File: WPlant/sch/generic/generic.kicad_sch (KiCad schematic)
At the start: 70 parts, among them J1 PROG/JTAG, J10 Ext, J8 eInk-Buttons, J9 Leak, M1 Motor_DC, Q5 PMOS, Q6 NPN, SW1 SW_Push, SW2 SW_Push, SW3 SW_Push, U1 SIWG917Y121MGABAR, U10 SP485EEN-L/TR, U11 TXU0102QDCURQ1, U5 TC4427AEOA713, U8 NC7S02P5, U9 INA180A2, X1 SIT1552AI-JE-DCC-32.768D

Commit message: Update WP Extension and Generic
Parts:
- removed Q5: PMOS, symbol Simulation_SPICE:PMOS
- removed Q6: NPN, symbol Simulation_SPICE:NPN
- added Q6: Si2301, Package_TO_SOT_SMD:SOT-23, symbol Device:Q_PMOS_GSD
- added Q7: BC817, Package_TO_SOT_SMD:SOT-23, symbol Transistor_BJT:BC817
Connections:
- net GND: now also Q7.2 (E)
- net VBUS: now also Q6.2 (S)
- net at R36.1: now also Q6.3 (D)
- net at R38.1: now also Q6.1 (G), Q7.3 (C)
- net at R39.1: now also Q7.1 (B)
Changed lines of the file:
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@@
 	)
 	(symbol
-		(lib_id "Simulation_SPICE:PMOS")
-		(at 66.04 149.86 270)
-		(mirror x)
-		(unit 1)
-		(exclude_from_sim no)
-		(in_bom yes)
-		(on_board yes)
-		(dnp no)
-		(property "Reference" "Q5"
-			(at 66.04 140.97 90)
-			(effects
-				(font
-					(size 1.27 1.27)
-				)
-			)
-		)
-		(property "Value" "PMOS"
-			(at 66.04 143.51 90)
-			(effects
-				(font
-					(size 1.27 1.27)
-				)
-			)
-		)
-		(property "Footprint" ""
-			(at 68.58 144.78 0)
-			(effects
-				(font
-					(size 1.27 1.27)
-				)
-				(hide yes)
-			)
-		)
-		(property "Datasheet" "https://ngspice.sourceforge.io/docs/ngspice-html-manual/manual.xhtml#cha_MOSFETs"
-			(at 53.34 149.86 0)
-			(effects
-				(font
-					(size 1.27 1.27)
-				)
-				(hide yes)
-			)
-		)
-		(property "Description" "P-MOSFET transistor, drain/source/gate"
-			(at 66.04 149.86 0)
-			(effects
-				(font
-					(size 1.27 1.27)
-				)
-				(hide yes)
-			)
-		)
-		(property "Sim.Device" "PMOS"
-			(at 48.895 149.86 0)
-			(effects
-				(font
-					(size 1.27 1.27)
-				)
-				(hide yes)
-			)
-		)
-		(property "Sim.Type" "VDMOS"
-			(at 46.99 149.86 0)
-			(effects
-				(font
-					(size 1.27 1.27)
-				)
-				(hide yes)
-			)
-		)
-		(property "Sim.Pins" "1=D 2=G 3=S"
-			(at 50.8 149.86 0)
-			(effects
-				(font
-					(size 1.27 1.27)
-				)
-				(hide yes)
-			)
-		)
-		(pin "2"
-		)
-		(pin "1"
-		)
-		(pin "3"
-		)
-		(instances
-			(project ""
-				(path "/71bd3f7f-463d-4a2c-bec7-ca56c2fe6cec"
-					(reference "Q5")
-					(unit 1)
-				)
-			)
-		)
-	)
-	(symbol
 		(lib_id "Device:R")
 		(at 190.5 97.79 90)
@@
 	)
 	(symbol
-		(lib_id "Simulation_SPICE:NPN")
-		(at 29.21 171.45 0)
-		(unit 1)
-		(exclude_from_sim no)
-		(in_bom yes)
-		(on_board yes)
-		(dnp no)
-		(fields_autoplaced yes)
-		(property "Reference" "Q6"
-			(at 34.29 170.1799 0)
-			(effects
-				(font
-					(size 1.27 1.27)
-				)
-				(justify left)
-			)
-		)
-		(property "Value" "NPN"
-			(at 34.29 172.7199 0)
-			(effects
-				(font
-					(size 1.27 1.27)
-				)
-				(justify left)
-			)
-		)
-		(property "Footprint" ""
-			(at 92.71 171.45 0)
-			(effects
-				(font
-					(size 1.27 1.27)
-				)
-				(hide yes)
-			)
-		)
-		(property "Datasheet" "https://ngspice.sourceforge.io/docs/ngspice-html-manual/manual.xhtml#cha_BJTs"
-			(at 92.71 171.45 0)
-			(effects
-				(font
-					(size 1.27 1.27)
-				)
-				(hide yes)
-			)
-		)
-		(property "Description" "Bipolar transistor symbol for simulation only, substrate tied to the emitter"
-			(at 29.21 171.45 0)
-			(effects
-				(font
-					(size 1.27 1.27)
-				)
-				(hide yes)
-			)
-		)
-		(property "Sim.Device" "NPN"
-			(at 29.21 171.45 0)
-			(effects
-				(font
-					(size 1.27 1.27)
-				)
-				(hide yes)
-			)
-		)
-		(property "Sim.Type" "GUMMELPOON"
-			(at 29.21 171.45 0)
-			(effects
-				(font
-					(size 1.27 1.27)
-				)
-				(hide yes)
-			)
-		)
-		(property "Sim.Pins" "1=C 2=B 3=E"
-			(at 29.21 171.45 0)
-			(effects
-				(font
-					(size 1.27 1.27)
-				)
-				(hide yes)
-			)
-		)
-		(pin "3"
-		)
-		(pin "1"
-		)
-		(pin "2"
-		)
-		(instances
-			(project ""
-				(path "/71bd3f7f-463d-4a2c-bec7-ca56c2fe6cec"
-					(reference "Q6")
-					(unit 1)
-				)
-			)
-		)
-	)
-	(symbol
 		(lib_id "power:+3.3V")
 		(at 52.07 88.9 270)
@@
 	)
 	(symbol
+		(lib_id "Device:Q_PMOS_GSD")
+		(at 66.04 149.86 270)
+		(mirror x)
+		(unit 1)
+		(exclude_from_sim no)
+		(in_bom yes)
+		(on_board yes)
+		(dnp no)
+		(property "Reference" "Q6"
+			(at 66.04 140.97 90)
+			(effects
+				(font
+					(size 1.27 1.27)
+				)
+			)
+		)
+		(property "Value" "Si2301"
+			(at 66.04 143.51 90)
+			(effects
+				(font
+					(size 1.27 1.27)
+				)
+			)
+		)
+		(property "Footprint" "Package_TO_SOT_SMD:SOT-23"
+			(at 68.58 144.78 0)
+			(effects
+				(font
+					(size 1.27 1.27)
+				)
+				(hide yes)
+			)
+		)
+		(property "Datasheet" "~"
+			(at 66.04 149.86 0)
+			(effects
+				(font
+					(size 1.27 1.27)
+				)
+				(hide yes)
+			)
+		)
+		(property "Description" "P-MOSFET transistor, gate/source/drain"
+			(at 66.04 149.86 0)
+			(effects
+				(font
+					(size 1.27 1.27)
+				)
+				(hide yes)
+			)
+		)
+		(pin "2"
+		)
+		(pin "1"
+		)
+		(pin "3"
+		)
+		(instances
+			(project ""
+				(path "/71bd3f7f-463d-4a2c-bec7-ca56c2fe6cec"
+					(reference "Q6")
+					(unit 1)
+				)
+			)
+		)
+	)
+	(symbol
 		(lib_id "power:+3.3V")
 		(at 39.37 19.05 0)
@@
 					(unit 1)
 				)
+			)
+		)
+	)
+	(symbol
+		(lib_id "Transistor_BJT:BC817")
+		(at 29.21 171.45 0)
+		(unit 1)
+		(exclude_from_sim no)
+		(in_bom yes)
+		(on_board yes)
+		(dnp no)
+		(property "Reference" "Q7"
+			(at 34.798 169.672 0)
+			(effects
+				(font
+					(size 1.27 1.27)
+				)
+				(justify left)
+			)
+		)
+		(property "Value" "BC817"
+			(at 33.782 174.498 0)
+			(effects
+				(font
+					(size 1.27 1.27)
+				)
+				(justify left)
+			)
+		)
+		(property "Footprint" "Package_TO_SOT_SMD:SOT-23"
+			(at 34.29 173.355 0)
+			(effects
+				(font
+					(size 1.27 1.27)
+					(italic yes)
+				)
+				(justify left)
+				(hide yes)
+			)
+		)
+		(property "Datasheet" "https://www.onsemi.com/pub/Collateral/BC818-D.pdf"
+			(at 29.21 171.45 0)
+			(effects
+				(font
+					(size 1.27 1.27)
+				)
+				(justify left)
+				(hide yes)
+			)
+		)
+		(property "Description" "0.8A Ic, 45V Vce, NPN Transistor, SOT-23"
+			(at 29.21 171.45 0)
+			(effects
+				(font
+					(size 1.27 1.27)
+				)
+				(hide yes)
+			)
+		)
+		(pin "1"
+		)
+		(pin "2"
+		)
+		(pin "3"
+		)
+		(instances
+			(project ""
+				(path "/71bd3f7f-463d-4a2c-bec7-ca56c2fe6cec"
+					(reference "Q7")
+					(unit 1)
+				)

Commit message: Almost finished WP Generic
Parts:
- C1, C2, C3, C30, C31, C32, C33, C35, C36, C37, C38, C39, C4, C5, C6, C7, C8, C9: footprint (none) -> Capacitor_SMD:C_0603_1608Metric_Pad1.08x0.95mm_HandSolder
- D1, D2: footprint (none) -> LED_THT:LED_D5.0mm
- D10: footprint (none) -> Diode_SMD:D_SMC
- J1: footprint (none) -> Connector_PinHeader_2.54mm:PinHeader_2x06_P2.54mm_Horizontal
- J10: footprint (none) -> local:CONN-TH_4
- J9: footprint (none) -> Connector_PinHeader_2.54mm:PinHeader_1x02_P2.54mm_Vertical
- M1: footprint (none) -> Connector_JST:JST_XH_B2B-XH-A_1x02_P2.50mm_Vertical
- R1, R19, R2, R21, R22, R3, R32, R33, R34, R35, R36, R37, R38, R39, R4, R41, R42, R43, R48, R49, R5, R6, R7, R8, R9: footprint (none) -> Resistor_SMD:R_0603_1608Metric_Pad0.98x0.95mm_HandSolder
- R31: footprint (none) -> Resistor_SMD:R_Shunt_Vishay_WSK2512_6332Metric_T2.21mm
- SW1, SW2, SW3: footprint (none) -> local:KEY-TH_2P-L6.0-W3.5-P6.50
- TP1, TP2, TP3, TP4, TP5: footprint (none) -> TestPoint:TestPoint_Pad_1.0x1.0mm
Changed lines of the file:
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@@
 			)
 		)
-		(property "Footprint" ""
+		(property "Footprint" "Resistor_SMD:R_0603_1608Metric_Pad0.98x0.95mm_HandSolder"
 			(at 120.65 67.818 90)
 			(effects
@@
 			)
 		)
-		(property "Footprint" ""
+		(property "Footprint" "local:CONN-TH_4"
 			(at 252.73 26.67 0)
 			(effects
@@
 			)
 		)
-		(property "Footprint" ""
+		(property "Footprint" "LED_THT:LED_D5.0mm"
 			(at 201.93 113.03 0)
 			(effects
@@
 			)
 		)
-		(property "Footprint" ""
+		(property "Footprint" "Capacitor_SMD:C_0603_1608Metric_Pad1.08x0.95mm_HandSolder"
 			(at 48.5648 177.8 0)
 			(effects
@@
 			)
 		)
-		(property "Footprint" ""
+		(property "Footprint" "Capacitor_SMD:C_0603_1608Metric_Pad1.08x0.95mm_HandSolder"
 			(at 115.2652 59.69 0)
 			(effects
@@
 			)
 		)
-		(property "Footprint" ""
+		(property "Footprint" "Resistor_SMD:R_0603_1608Metric_Pad0.98x0.95mm_HandSolder"
 			(at 233.68 38.608 90)
 			(effects
@@
 			)
 		)
-		(property "Footprint" ""
+		(property "Footprint" "local:KEY-TH_2P-L6.0-W3.5-P6.50"
 			(at 26.67 115.57 0)
 			(effects
@@
 			)
 		)
-		(property "Footprint" ""
+		(property "Footprint" "Resistor_SMD:R_0603_1608Metric_Pad0.98x0.95mm_HandSolder"
 			(at 190.5 99.568 90)
 			(effects
@@
 			)
 		)
-		(property "Footprint" ""
+		(property "Footprint" "Capacitor_SMD:C_0603_1608Metric_Pad1.08x0.95mm_HandSolder"
 			(at 77.1652 35.56 0)
 			(effects
@@
 			)
 		)
-		(property "Footprint" ""
+		(property "Footprint" "local:KEY-TH_2P-L6.0-W3.5-P6.50"
 			(at 26.67 109.22 0)
 			(effects
@@
 			)
 		)
-		(property "Footprint" ""
+		(property "Footprint" "LED_THT:LED_D5.0mm"
 			(at 201.93 105.41 0)
 			(effects
@@
 			)
 		)
-		(property "Footprint" ""
+		(property "Footprint" "Capacitor_SMD:C_0603_1608Metric_Pad1.08x0.95mm_HandSolder"
 			(at 53.0352 35.56 0)
 			(effects
@@
 			)
 		)
-		(property "Footprint" ""
+		(property "Footprint" "Capacitor_SMD:C_0603_1608Metric_Pad1.08x0.95mm_HandSolder"
 			(at 112.7252 30.48 0)
 			(effects
@@
 			)
 		)
-		(property "Footprint" ""
+		(property "Footprint" "Connector_JST:JST_XH_B2B-XH-A_1x02_P2.50mm_Vertical"
 			(at 267.97 124.206 0)
 			(effects
@@
 			)
 		)
-		(property "Footprint" ""
+		(property "Footprint" "Connector_PinHeader_2.54mm:PinHeader_1x02_P2.54mm_Vertical"
 			(at 100.33 113.03 0)
 			(effects
@@
 			)
 		)
-		(property "Footprint" ""
+		(property "Footprint" "TestPoint:TestPoint_Pad_1.0x1.0mm"
 			(at 186.69 115.57 0)
 			(effects
@@
 			)
 		)
-		(property "Footprint" ""
+		(property "Footprint" "Resistor_SMD:R_0603_1608Metric_Pad0.98x0.95mm_HandSolder"
 			(at 234.95 17.018 90)
 			(effects
@@
 			)
 		)
-		(property "Footprint" ""
+		(property "Footprint" "Capacitor_SMD:C_0603_1608Metric_Pad1.08x0.95mm_HandSolder"
 			(at 125.73 188.2648 0)
 			(effects
@@
 			)
 		)
-		(property "Footprint" ""
+		(property "Footprint" "Resistor_SMD:R_0603_1608Metric_Pad0.98x0.95mm_HandSolder"
 			(at 199.39 30.988 90)
 			(effects
@@
 			)
 		)
-		(property "Footprint" ""
+		(property "Footprint" "Resistor_SMD:R_0603_1608Metric_Pad0.98x0.95mm_HandSolder"
 			(at 72.898 59.69 90)
 			(effects
@@
 			)
 		)
-		(property "Footprint" ""
+		(property "Footprint" "Resistor_SMD:R_0603_1608Metric_Pad0.98x0.95mm_HandSolder"
 			(at 190.5 114.808 90)
 			(effects
@@
 			)
 		)
-		(property "Footprint" ""
+		(property "Footprint" "TestPoint:TestPoint_Pad_1.0x1.0mm"
 			(at 179.07 87.63 0)
 			(effects
@@
 			)
 		)
-		(property "Footprint" ""
+		(property "Footprint" "Resistor_SMD:R_0603_1608Metric_Pad0.98x0.95mm_HandSolder"
 			(at 195.58 56.388 90)
 			(effects
@@
 			)
 		)
-		(property "Footprint" ""
+		(property "Footprint" "Capacitor_SMD:C_0603_1608Metric_Pad1.08x0.95mm_HandSolder"
 			(at 88.5952 35.56 0)
 			(effects
@@
 			)
 		)
-		(property "Footprint" ""
+		(property "Footprint" "Connector_PinHeader_2.54mm:PinHeader_2x06_P2.54mm_Horizontal"
 			(at 41.91 81.28 0)
 			(effects
@@
 			)
 		)
-		(property "Footprint" ""
+		(property "Footprint" "Capacitor_SMD:C_0603_1608Metric_Pad1.08x0.95mm_HandSolder"
 			(at 65.7352 35.56 0)
 			(effects
@@
 			)
 		)
-		(property "Footprint" ""
+		(property "Footprint" "Capacitor_SMD:C_0603_1608Metric_Pad1.08x0.95mm_HandSolder"
 			(at 101.2952 30.48 0)
 			(effects
@@
 			)
 		)
-		(property "Footprint" ""
+		(property "Footprint" "Resistor_SMD:R_0603_1608Metric_Pad0.98x0.95mm_HandSolder"
 			(at 190.5 102.108 90)
 			(effects
@@
 			)
 		)
-		(property "Footprint" ""
+		(property "Footprint" "Capacitor_SMD:C_0603_1608Metric_Pad1.08x0.95mm_HandSolder"
 			(at 101.2952 82.55 0)
 			(effects
@@
 			)
 		)
-		(property "Footprint" ""
+		(property "Footprint" "Capacitor_SMD:C_0603_1608Metric_Pad1.08x0.95mm_HandSolder"
 			(at 104.14 46.0248 0)
 			(effects
@@
 			)
 		)
-		(property "Footprint" ""
+		(property "Footprint" "TestPoint:TestPoint_Pad_1.0x1.0mm"
 			(at 179.07 95.25 0)
 			(effects
@@
 			)
 		)
-		(property "Footprint" ""
+		(property "Footprint" "Resistor_SMD:R_0603_1608Metric_Pad0.98x0.95mm_HandSolder"
 			(at 23.368 165.1 90)
 			(effects
@@
 			)
 		)
-		(property "Footprint" ""
+		(property "Footprint" "Resistor_SMD:R_Shunt_Vishay_WSK2512_6332Metric_T2.21mm"
 			(at 269.748 137.16 90)
 			(effects
@@
 			)
 		)
-		(property "Footprint" ""
+		(property "Footprint" "Resistor_SMD:R_0603_1608Metric_Pad0.98x0.95mm_HandSolder"
 			(at 190.5 104.648 90)
 			(effects
@@
 			)
 		)
-		(property "Footprint" ""
+		(property "Footprint" "Resistor_SMD:R_0603_1608Metric_Pad0.98x0.95mm_HandSolder"
 			(at 225.298 147.32 90)
 			(effects
@@
 			)
 		)
-		(property "Footprint" ""
+		(property "Footprint" "Resistor_SMD:R_0603_1608Metric_Pad0.98x0.95mm_HandSolder"
 			(at 190.5 107.188 90)
 			(effects
@@
 			)
 		)
-		(property "Footprint" ""
+		(property "Footprint" "Resistor_SMD:R_0603_1608Metric_Pad0.98x0.95mm_HandSolder"
 			(at 78.74 149.098 90)
 			(effects
@@
 			)
 		)
-		(property "Footprint" ""
+		(property "Footprint" "Capacitor_SMD:C_0603_1608Metric_Pad1.08x0.95mm_HandSolder"
 			(at 59.69 101.9048 0)
 			(effects
@@
 			)
 		)
-		(property "Footprint" ""
+		(property "Footprint" "Resistor_SMD:R_0603_1608Metric_Pad0.98x0.95mm_HandSolder"
 			(at 190.5 76.708 90)
 			(effects
@@
 			)
 		)
-		(property "Footprint" ""
+		(property "Footprint" "Diode_SMD:D_SMC"
 			(at 275.59 123.19 0)
 			(effects
@@
 			)
 		)
-		(property "Footprint" ""
+		(property "Footprint" "Capacitor_SMD:C_0603_1608Metric_Pad1.08x0.95mm_HandSolder"
 			(at 263.8552 30.48 0)
 			(effects
@@
 			)
 		)
-		(property "Footprint" ""
+		(property "Footprint" "TestPoint:TestPoint_Pad_1.0x1.0mm"
 			(at 115.57 102.87 0)
 			(effects
@@
 			)
 		)
-		(property "Footprint" ""
+		(property "Footprint" "Resistor_SMD:R_0603_1608Metric_Pad0.98x0.95mm_HandSolder"
 			(at 189.23 69.088 90)
 			(effects
@@
 			)
 		)
-		(property "Footprint" ""
+		(property "Footprint" "Resistor_SMD:R_0603_1608Metric_Pad0.98x0.95mm_HandSolder"
 			(at 58.928 153.67 90)
 			(effects
@@
 			)
 		)
-		(property "Footprint" ""
+		(property "Footprint" "Capacitor_SMD:C_0603_1608Metric_Pad1.08x0.95mm_HandSolder"
 			(at 238.4552 156.21 0)
 			(effects
@@
 			)
 		)
-		(property "Footprint" ""
+		(property "Footprint" "Resistor_SMD:R_0603_1608Metric_Pad0.98x0.95mm_HandSolder"
 			(at 90.17 149.098 90)
 			(effects
@@
 			)
 		)
-		(property "Footprint" ""
+		(property "Footprint" "Resistor_SMD:R_0603_1608Metric_Pad0.98x0.95mm_HandSolder"
 			(at 194.31 33.528 90)
 			(effects
@@
 			)
 		)
-		(property "Footprint" ""
+		(property "Footprint" "Resistor_SMD:R_0603_1608Metric_Pad0.98x0.95mm_HandSolder"
 			(at 224.79 17.018 90)
 			(effects
@@
 			)
 		)
-		(property "Footprint" ""
+		(property "Footprint" "Resistor_SMD:R_0603_1608Metric_Pad0.98x0.95mm_HandSolder"
 			(at 106.68 121.158 90)
 			(effects
@@
 			)
 		)
-		(property "Footprint" ""
+		(property "Footprint" "Capacitor_SMD:C_0603_1608Metric_Pad1.08x0.95mm_HandSolder"
 			(at 40.3352 35.56 0)
 			(effects
@@
 			)
 		)
-		(property "Footprint" ""
+		(property "Footprint" "Resistor_SMD:R_0603_1608Metric_Pad0.98x0.95mm_HandSolder"
 			(at 107.95 90.678 90)
 			(effects
@@
 			)
 		)
-		(property "Footprint" ""
+		(property "Footprint" "Resistor_SMD:R_0603_1608Metric_Pad0.98x0.95mm_HandSolder"
 			(at 92.71 85.598 90)
 			(effects
@@
 			)
 		)
-		(property "Footprint" ""
+		(property "Footprint" "TestPoint:TestPoint_Pad_1.0x1.0mm"
 			(at 186.69 120.65 0)
 			(effects
@@
 			)
 		)
-		(property "Footprint" ""
+		(property "Footprint" "Resistor_SMD:R_0603_1608Metric_Pad0.98x0.95mm_HandSolder"
 			(at 232.41 138.938 90)
 			(effects
@@
 			)
 		)
-		(property "Footprint" ""
+		(property "Footprint" "Capacitor_SMD:C_0603_1608Metric_Pad1.08x0.95mm_HandSolder"
 			(at 72.0852 80.01 0)
 			(effects
@@
 			)
 		)
-		(property "Footprint" ""
+		(property "Footprint" "Capacitor_SMD:C_0603_1608Metric_Pad1.08x0.95mm_HandSolder"
 			(at 213.0552 151.13 0)
 			(effects
@@
 			)
 		)
-		(property "Footprint" ""
+		(property "Footprint" "local:KEY-TH_2P-L6.0-W3.5-P6.50"
 			(at 26.67 121.92 0)
 			(effects
@@
 			)
 		)
-		(property "Footprint" ""
+		(property "Footprint" "Capacitor_SMD:C_0603_1608Metric_Pad1.08x0.95mm_HandSolder"
 			(at 146.05 175.5648 0)
 			(effects
@@
 			)
 		)
-		(property "Footprint" ""
+		(property "Footprint" "Resistor_SMD:R_0603_1608Metric_Pad0.98x0.95mm_HandSolder"
 			(at 190.5 79.248 90)
 			(effects

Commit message: Added 'local' lib
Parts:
- J10: footprint local:CONN-TH_4 -> locals:CONN-TH_DB301R-3.5-4P-GN-S
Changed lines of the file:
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@@
 			)
 		)
-		(property "Footprint" "local:CONN-TH_4"
+		(property "Footprint" "locals:CONN-TH_DB301R-3.5-4P-GN-S"
 			(at 252.73 26.67 0)
 			(effects

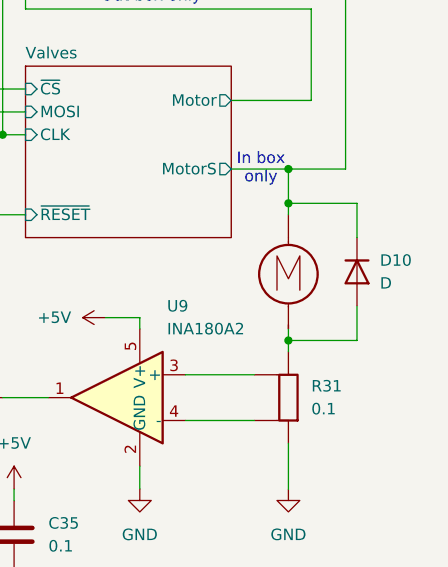
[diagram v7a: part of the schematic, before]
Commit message: Update WP Generic packages assignment
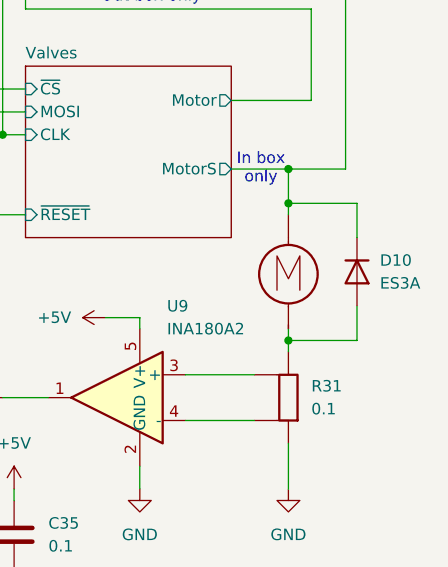
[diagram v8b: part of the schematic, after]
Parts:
- D10: value D -> ES3A
- J8: footprint (none) -> easyeda2kicad:CONN-TH_XAD-12A
- SW1, SW2, SW3: footprint local:KEY-TH_2P-L6.0-W3.5-P6.50 -> locals:KEY-TH_2P-L6.0-W3.5-P6.50
- U8: footprint easyeda2kicad:SC-70-5_L2.1-W1.3-P0.65-LS2.1-BL -> Package_TO_SOT_SMD:SOT-23-5_HandSoldering
- U9: footprint Package_TO_SOT_SMD:SOT-23-5 -> Package_TO_SOT_SMD:SOT-23-5_HandSoldering
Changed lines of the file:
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@@
 			)
 		)
-		(property "Footprint" "local:KEY-TH_2P-L6.0-W3.5-P6.50"
+		(property "Footprint" "locals:KEY-TH_2P-L6.0-W3.5-P6.50"
 			(at 26.67 115.57 0)
 			(effects
@@
 			)
 		)
-		(property "Footprint" "local:KEY-TH_2P-L6.0-W3.5-P6.50"
+		(property "Footprint" "locals:KEY-TH_2P-L6.0-W3.5-P6.50"
 			(at 26.67 109.22 0)
 			(effects
@@
 			)
 		)
-		(property "Footprint" ""
+		(property "Footprint" "easyeda2kicad:CONN-TH_XAD-12A"
 			(at 255.27 57.15 0)
 			(effects
@@
 			)
 		)
-		(property "Value" "D"
+		(property "Value" "ES3A"
 			(at 278.13 124.4599 90)
 			(effects
@@
 			)
 		)
-		(property "Footprint" "Package_TO_SOT_SMD:SOT-23-5"
+		(property "Footprint" "Package_TO_SOT_SMD:SOT-23-5_HandSoldering"
 			(at 247.65 135.89 0)
 			(effects
@@
 			)
 		)
-		(property "Footprint" "easyeda2kicad:SC-70-5_L2.1-W1.3-P0.65-LS2.1-BL"
+		(property "Footprint" "Package_TO_SOT_SMD:SOT-23-5_HandSoldering"
 			(at 86.36 181.61 0)
 			(effects
@@
 			)
 		)
-		(property "Footprint" "local:KEY-TH_2P-L6.0-W3.5-P6.50"
+		(property "Footprint" "locals:KEY-TH_2P-L6.0-W3.5-P6.50"
 			(at 26.67 121.92 0)
 			(effects
